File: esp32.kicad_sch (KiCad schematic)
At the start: 30 parts, among them J2 TC2030-IDC, J3 Conn_01x04, J4 USB_C_Receptacle_USB2.0, SW1 TL3330AF260QG, SW2 TL3330AF260QG, U7 RT9080-33GJ5, U8 ESP32-S3-WROOM-1, Y2 32.768kHz

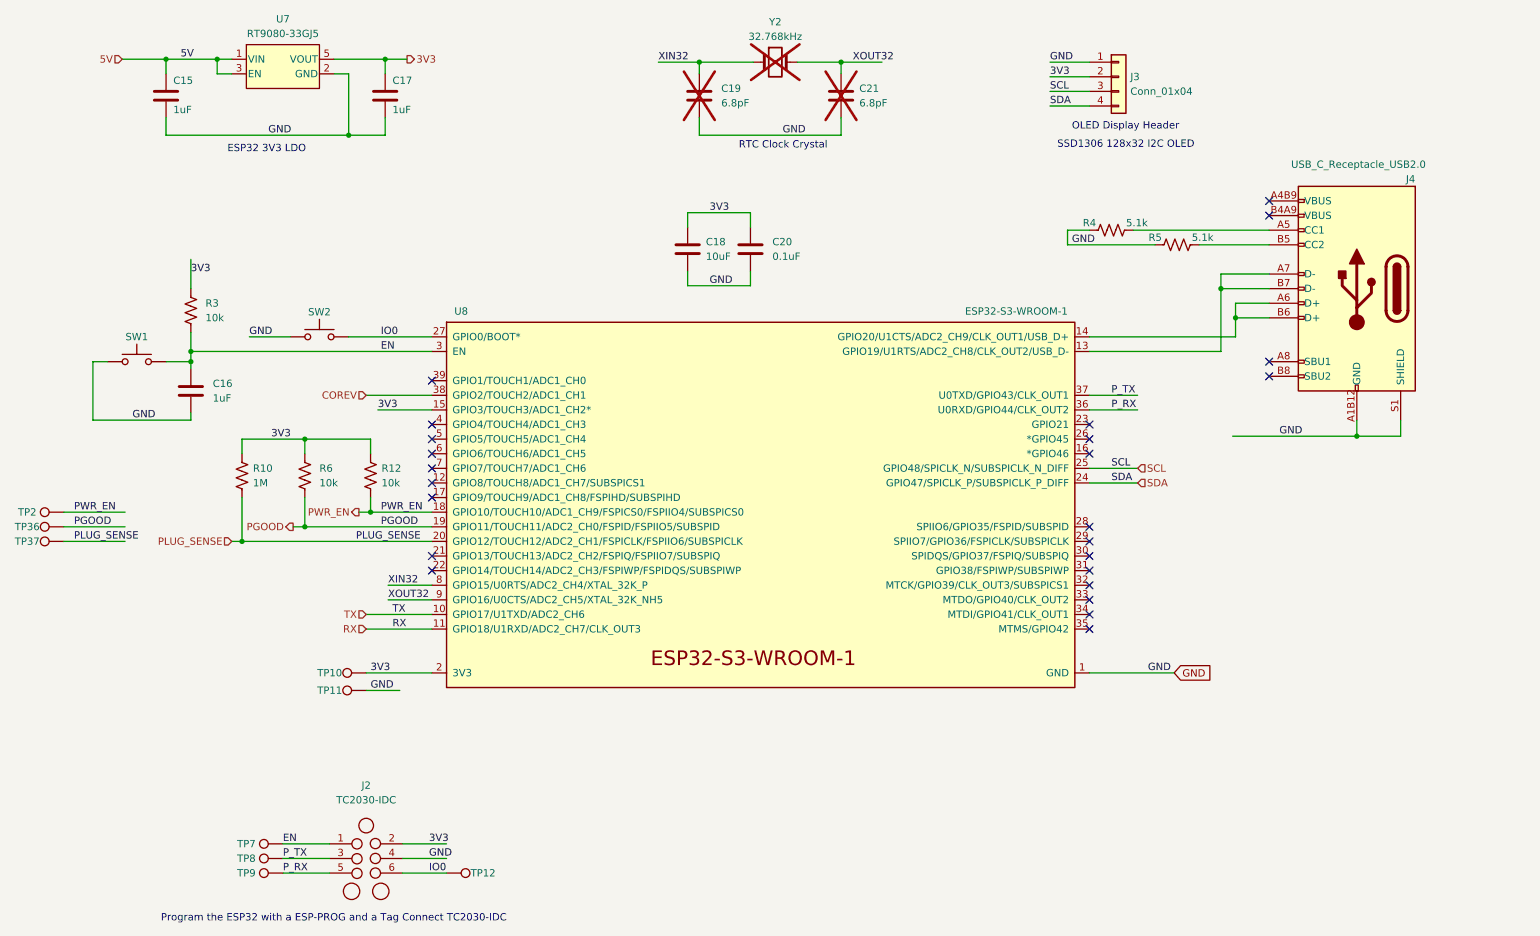
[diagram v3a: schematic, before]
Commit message: switch to bitaxeAura/GT base
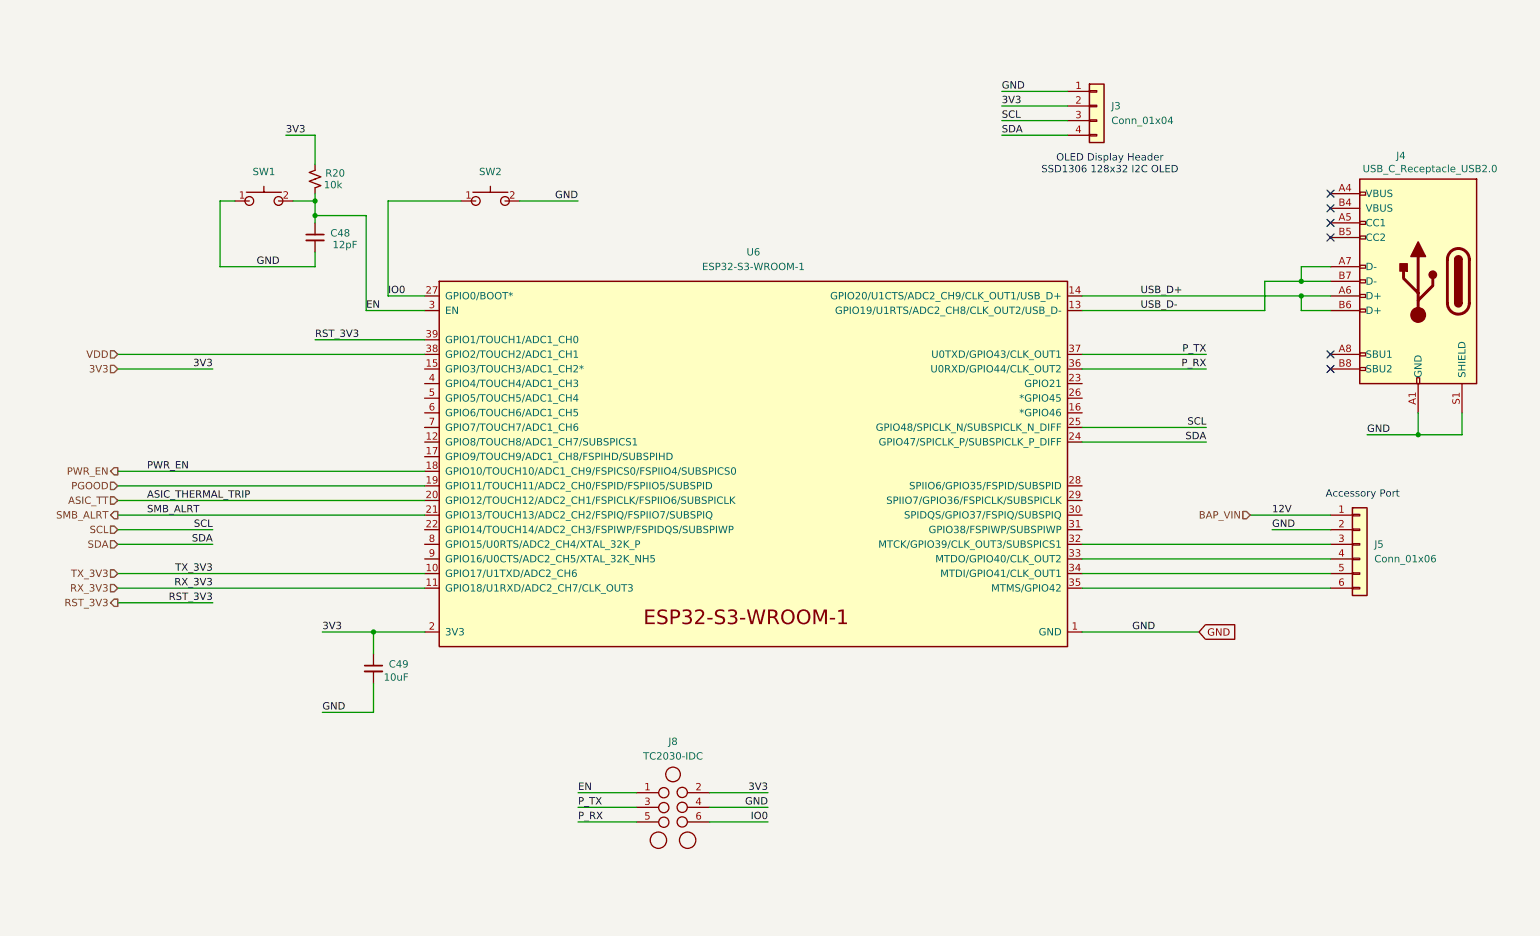
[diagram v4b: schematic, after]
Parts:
- removed C15, C16, C17: 1uF, Capacitor_SMD:C_0402_1005Metric, symbol Device:C
- removed C18: 10uF, Capacitor_SMD:C_0805_2012Metric, symbol Device:C
- removed C19, C21: 6.8pF, Capacitor_SMD:C_0402_1005Metric, symbol Device:C
- removed C20: 0.1uF, Capacitor_SMD:C_0402_1005Metric, symbol Device:C
- removed J2: TC2030-IDC, blockaxe:Tag-Connect_TC2030-IDC-NL_2x03_P1.27mm_Vertical, symbol blockaxe:TC2030-IDC-NL
- removed J4: USB_C_Receptacle_USB2.0, Connector_USB:USB_C_Receptacle_GCT_USB4105-xx-A_16P_TopMnt_Horizontal, symbol Connector:USB_C_Receptacle_USB2.0
- removed R10: 1M, Resistor_SMD:R_0402_1005Metric, symbol Device:R_US
- removed R12, R3, R6: 10k, Resistor_SMD:R_0402_1005Metric, symbol Device:R_US
- removed R4, R5: 5.1k, Resistor_SMD:R_0402_1005Metric, symbol Device:R_US
- removed SW1, SW2: TL3330AF260QG, blockaxe:SW_TL3330_EWI, symbol blockaxe:SW_Push
- removed TP10, TP11, TP12, TP2, TP36, TP37, TP7, TP8, TP9: TestPoint, TestPoint:TestPoint_Pad_D1.0mm, symbol Connector:TestPoint
- removed U7: RT9080-33GJ5, blockaxe:RT9080-33GJ5, symbol blockaxe:RT9080-33GJ5
- removed U8: ESP32-S3-WROOM-1, blockaxe:ESP32-S3-WROOM-1, symbol blockaxe:ESP32-S3-WROOM-1
- removed Y2: 32.768kHz, blockaxe:SC32S-7PF20PPM, symbol Device:Crystal
- added C48: 12pF, Capacitor_SMD:C_0402_1005Metric, symbol Device:C_Small
- added C49: 10uF, Capacitor_SMD:C_0603_1608Metric, symbol Device:C_Small
- added J4: USB_C_Receptacle_USB2.0, bitaxe:USB_C_Receptacle_GCT_USB4105-xx-A, symbol bitaxe:USB_C_Receptacle_USB2.0
- added J5: Conn_01x06, Connector_PinHeader_2.54mm:PinHeader_1x06_P2.54mm_Vertical, symbol Connector_Generic:Conn_01x06
- added J8: TC2030-IDC, Connector:Tag-Connect_TC2030-IDC-NL_2x03_P1.27mm_Vertical, symbol bitaxe:TC2030-IDC-NL
- added R20: 10k, Resistor_SMD:R_0402_1005Metric, symbol Device:R_Small_US
- added SW1, SW2: SWITCH-SPST, bitaxe:SW_TL3336AF160Q, symbol bitaxe:SWITCH-SPST
- added U6: ESP32-S3-WROOM-1, bitaxe:ESP32-S3-WROOM-1, symbol bitaxe:ESP32-S3-WROOM-1
- J3: footprint Connector_PinSocket_2.54mm:PinSocket_1x04_P2.54mm_Vertical_SMD_Pin1Right -> bitaxe:PinHeader_1x04_P2.54mm_Vertical_shifted; DK NPTC041KFXC-RC -> (none)
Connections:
- net 3V3: now also C49.1, J8.2 (Pin_2), R20.2, U6.2 (3V3)
- net EN: now also C48.1, J8.1 (Pin_1), R20.1, SW1.2, U6.3 (EN)
- net GND: now also C48.2, C49.2, J4.A1 (GND), J4.B1 (GND), J4.S1 (SHIELD), J5.2 (Pin_2), J8.4 (Pin_4), SW1.1, SW2.2, U6.1 (GND), U6.40 (GND), U6.41 (GND)
- net IO0: now also J8.6 (Pin_6), SW2.1, U6.27 (GPIO0/BOOT*)
- net PGOOD: now also U6.19 (GPIO11/TOUCH11/ADC2_CH0/FSPID/FSPIIO5/SUBSPID)
- net PWR_EN: now also U6.18 (GPIO10/TOUCH10/ADC1_CH9/FSPICS0/FSPIIO4/SUBSPICS0)
- net P_RX: now also J8.5 (Pin_5), U6.36 (U0RXD/GPIO44/CLK_OUT2)
- net P_TX: now also J8.3 (Pin_3), U6.37 (U0TXD/GPIO43/CLK_OUT1)
- net SCL: now also U6.25 (GPIO48/SPICLK_N/SUBSPICLK_N_DIFF)
- net SDA: now also U6.24 (GPIO47/SPICLK_P/SUBSPICLK_P_DIFF)
- new net: J5.3 (Pin_3), U6.32 (MTCK/GPIO39/CLK_OUT3/SUBSPICS1)
- new net: J5.4 (Pin_4), U6.33 (MTDO/GPIO40/CLK_OUT2)
- new net: J5.5 (Pin_5), U6.34 (MTDI/GPIO41/CLK_OUT1)
- new net: J5.6 (Pin_6), U6.35 (MTMS/GPIO42)
- new net ASIC_TT: U6.20 (GPIO12/TOUCH12/ADC2_CH1/FSPICLK/FSPIIO6/SUBSPICLK)
- new net BAP_VIN: J5.1 (Pin_1)
- new net RST_3V3: U6.39 (GPIO1/TOUCH1/ADC1_CH0)
- new net RX_3V3: U6.11 (GPIO18/U1RXD/ADC2_CH7/CLK_OUT3)
- new net SMB_ALRT: U6.21 (GPIO13/TOUCH13/ADC2_CH2/FSPIQ/FSPIIO7/SUBSPIQ)
- new net TX_3V3: U6.10 (GPIO17/U1TXD/ADC2_CH6)
- new net USB_D+: J4.A6 (D+), J4.B6 (D+), U6.14 (GPIO20/U1CTS/ADC2_CH9/CLK_OUT1/USB_D+)
- new net USB_D-: J4.A7 (D-), J4.B7 (D-), U6.13 (GPIO19/U1RTS/ADC2_CH8/CLK_OUT2/USB_D-)
- new net VDD: U6.38 (GPIO2/TOUCH2/ADC1_CH1)
- no-connect marks 24 -> 6
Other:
- note added: "Accessory Port"
- note added: "OLED Display Header SSD1306 128x32 I2C OLED"
- note removed: "ESP32 3V3 LDO"
- note removed: "OLED Display Header"
- note removed: "Program the ESP32 with a ESP-PROG and a Tag Connect TC2030-IDC"
- note removed: "RTC Clock Crystal"
- note removed: "SSD1306 128x32 I2C OLED"
- title: blockaxe1 -> bitaxeBonanza

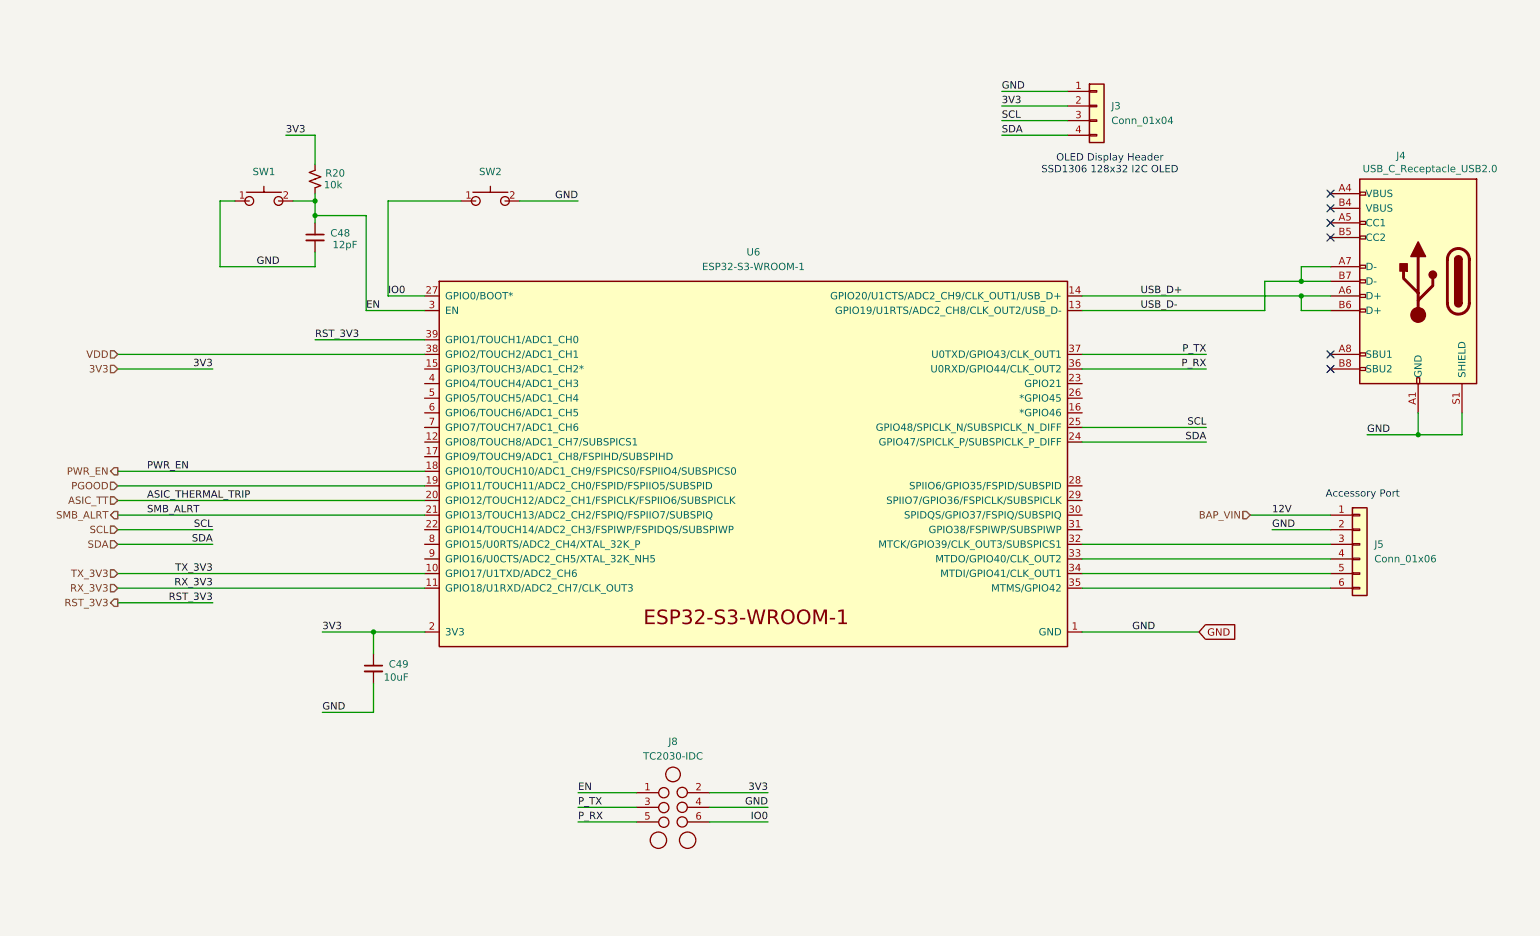
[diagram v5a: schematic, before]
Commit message: moved ASIC bypass caps out to separate sheet
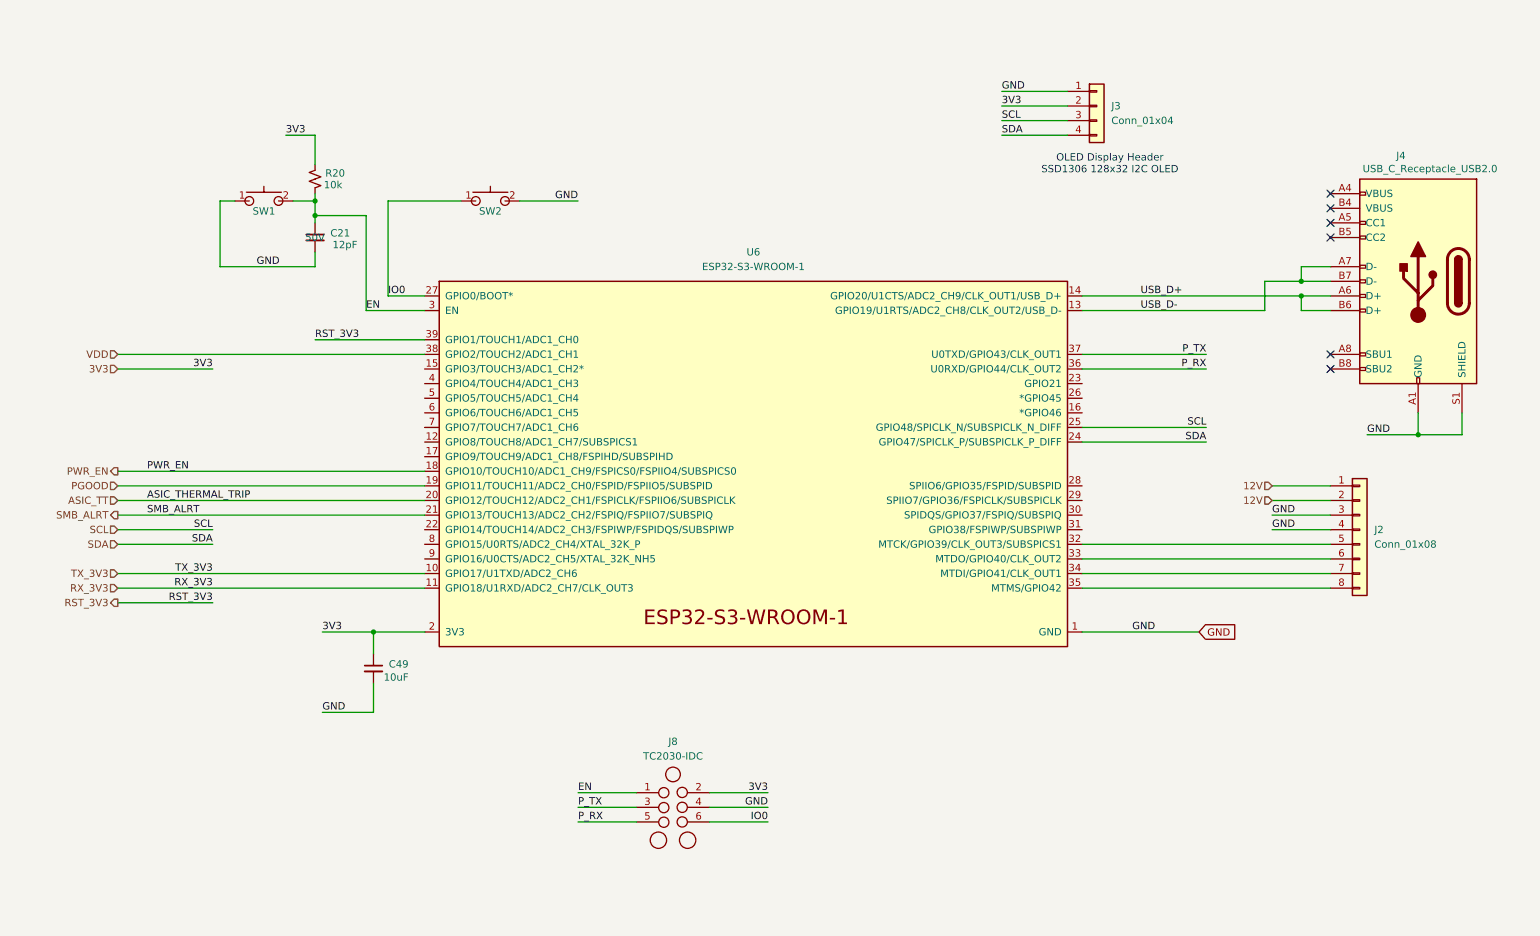
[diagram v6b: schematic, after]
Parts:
- removed J5: Conn_01x06, Connector_PinHeader_2.54mm:PinHeader_1x06_P2.54mm_Vertical, symbol Connector_Generic:Conn_01x06
- added J2: Conn_01x08, bitaxe:FPC-SMD_P0.50-8P_FGS-XJ-H2.0, symbol bitaxe:Conn_01x08-support
- C21: renamed from C48; Voltage (none) -> 50V; voltage 50V -> (none)
- SW1, SW2: footprint bitaxe:SW_TL3336AF160Q -> bitaxe:SW_TL3330AF130QG_EWI; DK 141-TL3336AF160QCT-ND -> EG4388CT-ND; PARTNO TL3336AF160Q -> TL3330AF130QG
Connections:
- net GND: now also J2.3 (Pin_3), J2.4 (Pin_4)
- net at U6.32 (MTCK/GPIO39/CLK_OUT3/SUBSPICS1): now also J2.5 (Pin_5)
- net at U6.33 (MTDO/GPIO40/CLK_OUT2): now also J2.6 (Pin_6)
- net at U6.34 (MTDI/GPIO41/CLK_OUT1): now also J2.7 (Pin_7)
- net at U6.35 (MTMS/GPIO42): now also J2.8 (Pin_8)
- new net: SW2.3 (NC), SW2.4 (NC)
- new net: J2.10 (NC), J2.9 (NC)
- new net: SW1.3 (NC), SW1.4 (NC)
- new net 12V: J2.1 (Pin_1), J2.2 (Pin_2)
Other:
- note removed: "Accessory Port"

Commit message: made the board double wide. rough ASIC and vreg placement.
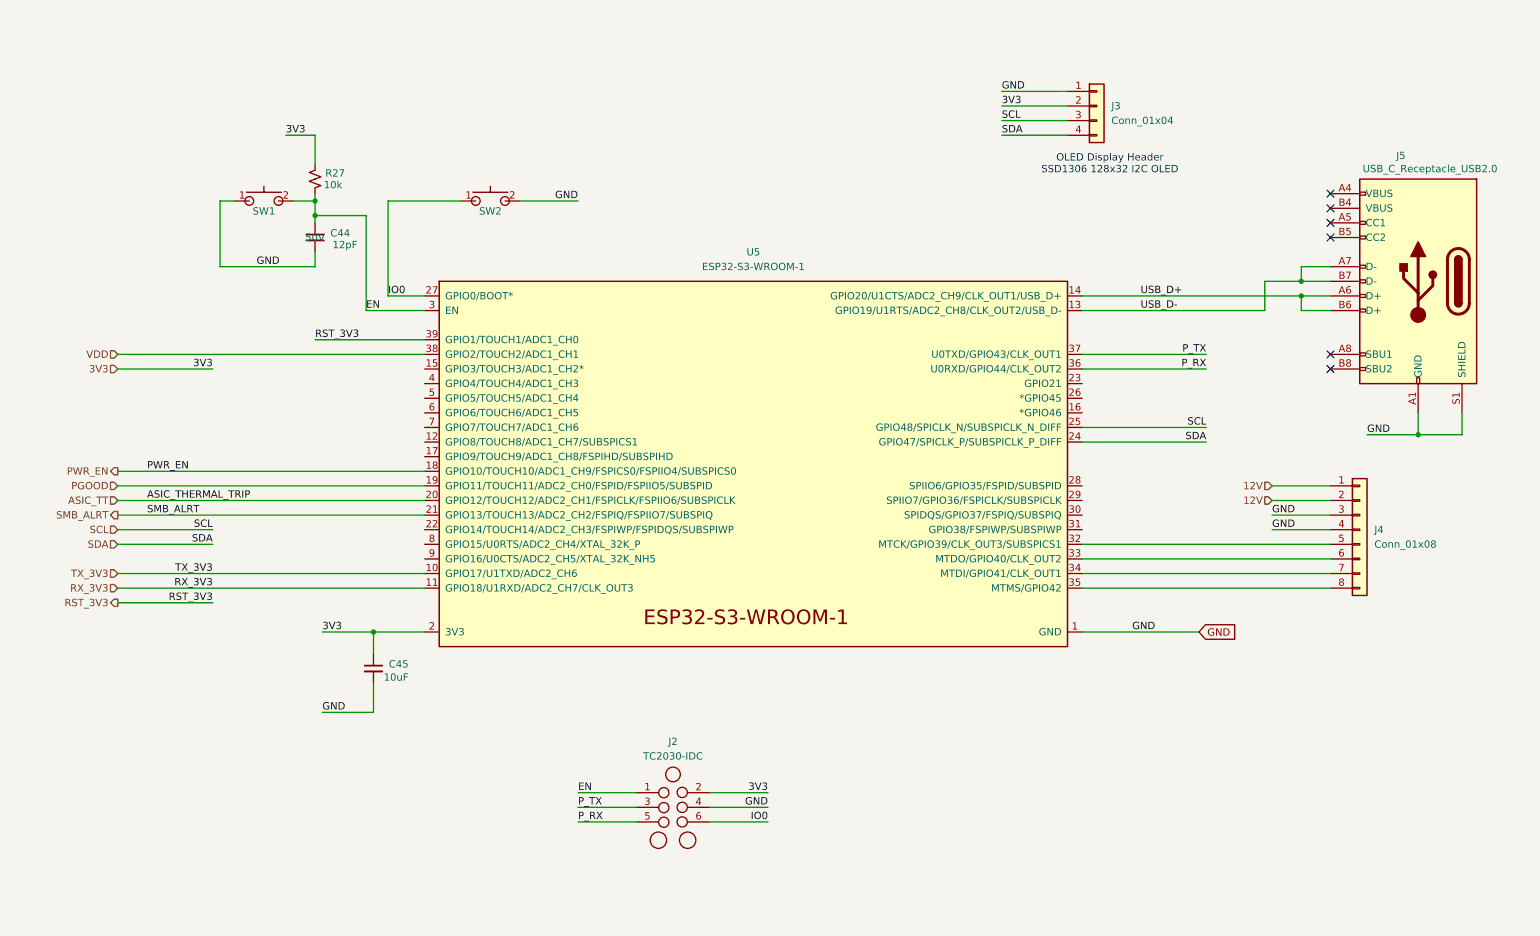
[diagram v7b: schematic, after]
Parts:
- renumbered C21 to C44, C49 to C45, J8 to J2, J2 to J4, J4 to J5, R20 to R27, U6 to U5
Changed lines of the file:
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@@
 		(dnp no)
 		(fields_autoplaced yes)
-		(property "Reference" "J8"
+		(property "Reference" "J2"
 			(at 128.27 146.05 0)
 			(effects
@@
 			(project ""
 				(path "/61fe8d2c-9301-4ad9-8caf-c47acfa835b0/0703810a-9d38-4b42-b83c-c94ab6e668a1"
-					(reference "J8")
+					(reference "J2")
 					(unit 1)
 				)
@@
 		(on_board yes)
 		(dnp no)
-		(property "Reference" "J2"
+		(property "Reference" "J4"
 			(at 250.19 109.2199 0)
 			(effects
@@
 			(project "BitaxeBonanza"
 				(path "/61fe8d2c-9301-4ad9-8caf-c47acfa835b0/0703810a-9d38-4b42-b83c-c94ab6e668a1"
-					(reference "J2")
+					(reference "J4")
 					(unit 1)
 				)
@@
 		(on_board yes)
 		(dnp no)
-		(property "Reference" "J4"
+		(property "Reference" "J5"
 			(at 254 44.196 0)
 			(effects
@@
 			(project ""
 				(path "/61fe8d2c-9301-4ad9-8caf-c47acfa835b0/0703810a-9d38-4b42-b83c-c94ab6e668a1"
-					(reference "J4")
+					(reference "J5")
 					(unit 1)
 				)
@@
 		(on_board yes)
 		(dnp no)
-		(property "Reference" "C49"
+		(property "Reference" "C45"
 			(at 82.296 132.588 0)
 			(effects
@@
 			(project "BitaxeGT"
 				(path "/61fe8d2c-9301-4ad9-8caf-c47acfa835b0/0703810a-9d38-4b42-b83c-c94ab6e668a1"
-					(reference "C49")
+					(reference "C45")
 					(unit 1)
 				)
@@
 		(dnp no)
 		(fields_autoplaced yes)
-		(property "Reference" "U6"
+		(property "Reference" "U5"
 			(at 142.24 60.96 0)
 			(effects
@@
 			(project ""
 				(path "/61fe8d2c-9301-4ad9-8caf-c47acfa835b0/0703810a-9d38-4b42-b83c-c94ab6e668a1"
-					(reference "U6")
+					(reference "U5")
 					(unit 1)
 				)
@@
 		(on_board yes)
 		(dnp no)
-		(property "Reference" "R20"
+		(property "Reference" "R27"
 			(at 67.818 47.244 0)
 			(effects
@@
 			(project "BitaxeBonanza"
 				(path "/61fe8d2c-9301-4ad9-8caf-c47acfa835b0/0703810a-9d38-4b42-b83c-c94ab6e668a1"
-					(reference "R20")
+					(reference "R27")
 					(unit 1)
 				)
@@
 		(on_board yes)
 		(dnp no)
-		(property "Reference" "C21"
+		(property "Reference" "C44"
 			(at 72.136 57.658 0)
 			(effects
@@
 			(project "BitaxeBonanza"
 				(path "/61fe8d2c-9301-4ad9-8caf-c47acfa835b0/0703810a-9d38-4b42-b83c-c94ab6e668a1"
-					(reference "C21")
+					(reference "C44")
 					(unit 1)
 				)
